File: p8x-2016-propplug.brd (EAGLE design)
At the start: 77.5 x 36.8 mm, 23 parts, among them CN1 USB_B, IC1 PIC18F24J50-I/P

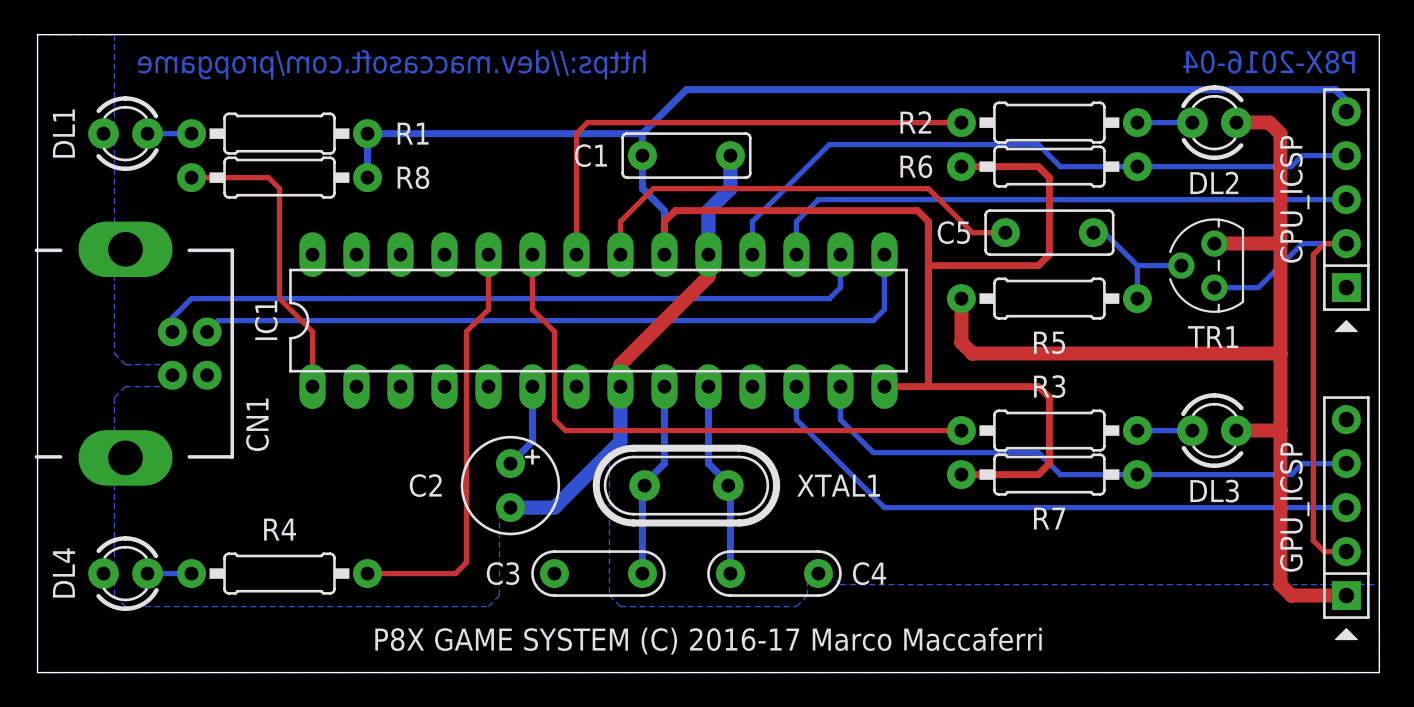
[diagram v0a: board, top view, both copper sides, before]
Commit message: Updates and fixes for PIC18F24J50
 * Fixed configuration bits
 * TX lines configured as open-drain and added pull-up resistors
 * UART initialization moved at startup
 * Speed optimizations
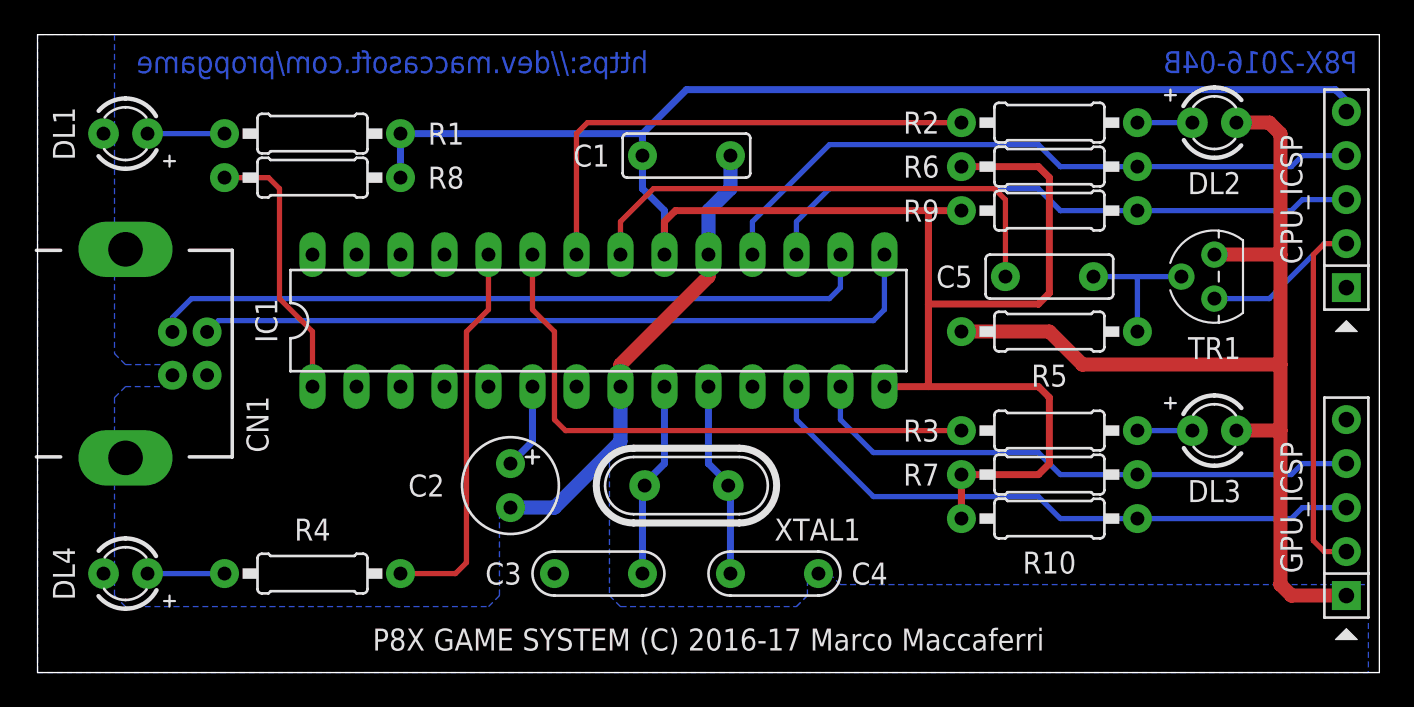
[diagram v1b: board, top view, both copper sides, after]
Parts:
- added R10, R9: 10.000, p8x-2016:0207/10
- moved C5 2.54 mm to (58.4, 22.9)
- moved R5 1.91 mm to (58.4, 19.7)
- moved R1 1.90 mm to (15.9, 31.1)
- moved R4 1.90 mm to (15.9, 5.71)
- moved R8 1.90 mm to (15.9, 28.6)
- moved TR1 0.64 mm to (67.9, 22.9)
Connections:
- net +3.3V: now also R10.2, R9.2
- net TX1: now also R9.1
- net TX2: now also R10.1
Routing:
- net +3.3V: track 131.7 -> 136.8 mm
- net !RES1!: track 26.0 -> 29.6 mm
- net GND: track 87.5 -> 85.5 mm
- net N$11: track 2.54 -> 4.45 mm
- net N$10: track 2.54 -> 4.45 mm
- net N$1: track 17.6 -> 15.7 mm
- net USB: track 24.3 -> 22.4 mm
- net TX1: track 34.2 -> 35.2 mm
- net TX2: track 35.8 -> 36.3 mm
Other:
- board text added: "P8X-2016-04B"
- board text removed: "P8X-2016-04"
